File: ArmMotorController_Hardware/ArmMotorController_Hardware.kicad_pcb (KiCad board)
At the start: 2 copper layers, 98 parts, among them SW1 SW_Push, SW2 SW_Push, SW3 SW_Push, SW4 SW_Push, SW5 SW_SPDT, U1 AP1059, U2 AP1059, U3 TM4C129E_Launchpad, U4 MAX_3232, U5 VNH5019A_E, U6 VNH5019A_E, U7 VNH5019A_E, U8 VNH5019A_E

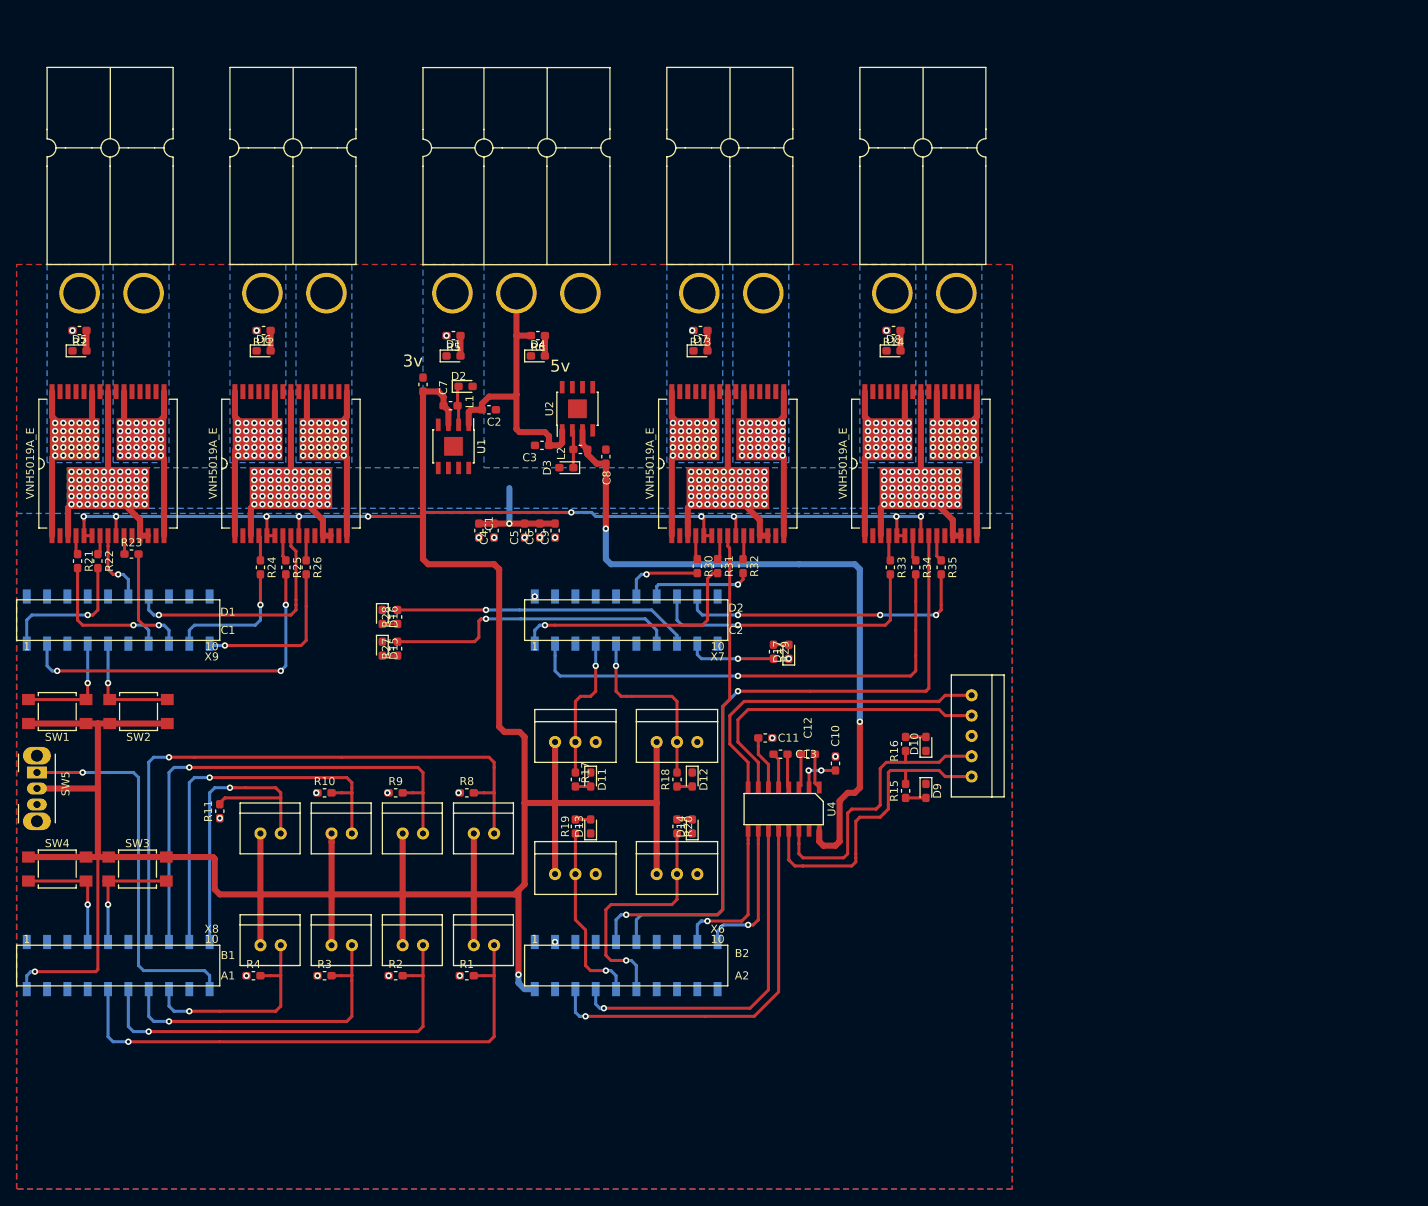
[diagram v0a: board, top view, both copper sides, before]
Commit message: Added text above the VNH's
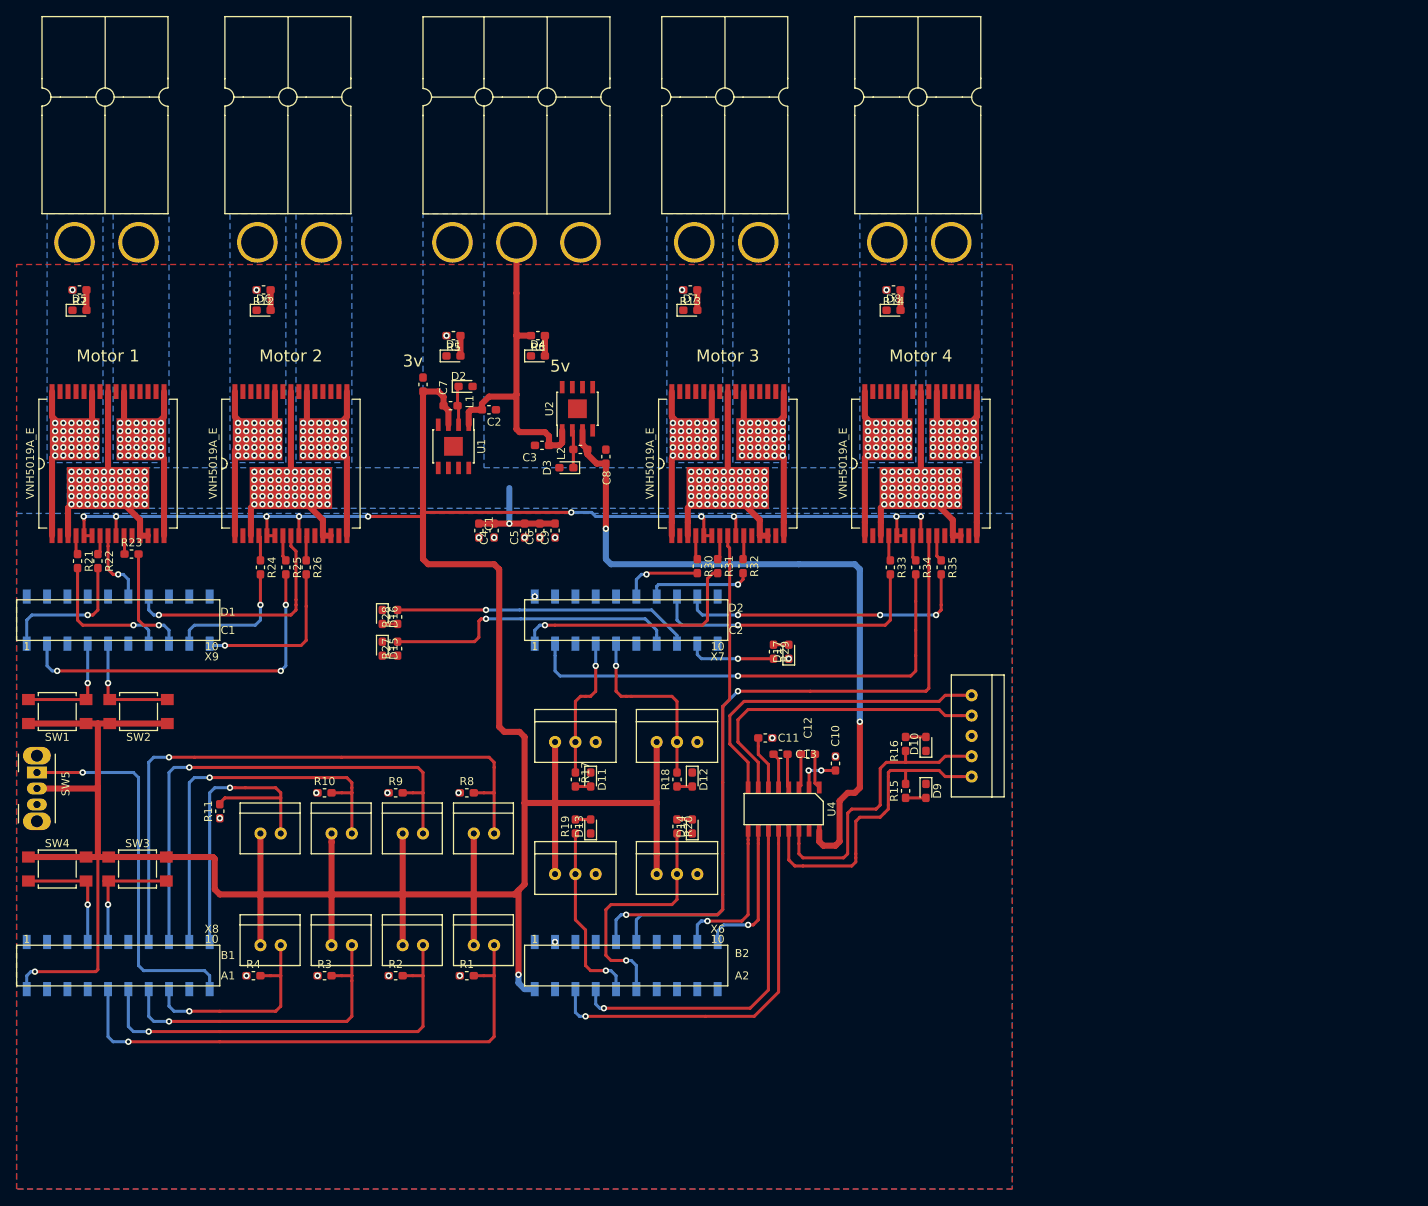
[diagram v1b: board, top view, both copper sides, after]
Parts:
- moved Conn17 6.38 mm to (65.4, 41.9)
- moved Conn18 6.38 mm to (120.0, 41.9)
- moved Conn16 6.38 mm to (42.5, 41.9)
- moved Conn19 6.38 mm to (144.1, 41.9)
- moved Conn1 6.35 mm to (90.2, 41.9)
- moved D7 5.24 mm to (123.6, 54.0)
- moved R13 5.24 mm to (123.6, 51.4)
- moved D5 5.08 mm to (47.2, 54.0)
- moved D6 5.08 mm to (70.2, 54.0)
- moved D8 5.08 mm to (149.0, 54.0)
- moved R12 5.08 mm to (70.2, 51.4)
- moved R14 5.08 mm to (149.0, 51.4)
- moved R7 5.08 mm to (47.2, 51.4)
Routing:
- net 12vLog: track 36.6 -> 43.0 mm
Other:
- board text added: "Motor 1"
- board text added: "Motor 2"
- board text added: "Motor 3"
- board text added: "Motor 4"

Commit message: save
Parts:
- moved D1 5.08 mm to (94.0, 54.6)
- moved R5 5.08 mm to (94.0, 52.1)
- moved D8 0.64 mm to (148.3, 54.0)
- moved R14 0.64 mm to (148.3, 51.4)
- moved D6 0.64 mm to (69.6, 54.0)
- moved D7 0.64 mm to (124.2, 54.0)
- moved R12 0.64 mm to (69.6, 51.4)
- moved R13 0.64 mm to (124.2, 51.4)
- moved D5 0.63 mm to (46.6, 54.0)
- moved R7 0.63 mm to (46.6, 51.4)
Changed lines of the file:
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@@
   )
   (setup
-    (last_trace_width 0.762)
+    (last_trace_width 0.25)
     (user_trace_width 0.254)
     (user_trace_width 0.381)
@@
   )
   (module Resistor_SMD:R_0603_1608Metric_Pad1.05x0.95mm_HandSolder (layer F.Cu)
-    (at 148.985 51.435 180)
+    (at 148.35 51.435 180)
     (descr "Resistor SMD 0603 (1608 Metric), square (rectangular) end terminal, IPC_7351 nominal with elongated pad for handsoldering. (Body size source: http://www.tortai-tech.com/upload/download/2011102023233369053.pdf), generated with kicad-footprint-generator")
     (tags "resistor handsolder")
@@
   )
   (module Resistor_SMD:R_0603_1608Metric_Pad1.05x0.95mm_HandSolder (layer F.Cu)
-    (at 123.585 51.435 180)
+    (at 124.22 51.435 180)
     (descr "Resistor SMD 0603 (1608 Metric), square (rectangular) end terminal, IPC_7351 nominal with elongated pad for handsoldering. (Body size source: http://www.tortai-tech.com/upload/download/2011102023233369053.pdf), generated with kicad-footprint-generator")
     (tags "resistor handsolder")
@@
   )
   (module Resistor_SMD:R_0603_1608Metric_Pad1.05x0.95mm_HandSolder (layer F.Cu)
-    (at 70.245 51.435 180)
+    (at 69.61 51.435 180)
     (descr "Resistor SMD 0603 (1608 Metric), square (rectangular) end terminal, IPC_7351 nominal with elongated pad for handsoldering. (Body size source: http://www.tortai-tech.com/upload/download/2011102023233369053.pdf), generated with kicad-footprint-generator")
     (tags "resistor handsolder")
@@
   )
   (module LED_SMD:LED_0603_1608Metric_Pad1.05x0.95mm_HandSolder (layer F.Cu)
-    (at 70.245 53.975)
+    (at 69.61 53.975)
     (descr "LED SMD 0603 (1608 Metric), square (rectangular) end terminal, IPC_7351 nominal, (Body size source: http://www.tortai-tech.com/upload/download/2011102023233369053.pdf), generated with kicad-footprint-generator")
     (tags "LED handsolder")
@@
   )
   (module LED_SMD:LED_0603_1608Metric_Pad1.05x0.95mm_HandSolder (layer F.Cu)
-    (at 148.985 53.975)
+    (at 148.35 53.975)
     (descr "LED SMD 0603 (1608 Metric), square (rectangular) end terminal, IPC_7351 nominal, (Body size source: http://www.tortai-tech.com/upload/download/2011102023233369053.pdf), generated with kicad-footprint-generator")
     (tags "LED handsolder")
@@
   )
   (module LED_SMD:LED_0603_1608Metric_Pad1.05x0.95mm_HandSolder (layer F.Cu)
-    (at 47.23 53.975)
+    (at 46.595 53.975)
     (descr "LED SMD 0603 (1608 Metric), square (rectangular) end terminal, IPC_7351 nominal, (Body size source: http://www.tortai-tech.com/upload/download/2011102023233369053.pdf), generated with kicad-footprint-generator")
     (tags "LED handsolder")
@@
   )
   (module LED_SMD:LED_0603_1608Metric_Pad1.05x0.95mm_HandSolder (layer F.Cu)
-    (at 123.585 53.975)
+    (at 124.22 53.975)
     (descr "LED SMD 0603 (1608 Metric), square (rectangular) end terminal, IPC_7351 nominal, (Body size source: http://www.tortai-tech.com/upload/download/2011102023233369053.pdf), generated with kicad-footprint-generator")
     (tags "LED handsolder")
@@
   )
   (module Resistor_SMD:R_0603_1608Metric_Pad1.05x0.95mm_HandSolder (layer F.Cu)
-    (at 93.98 57.15 180)
+    (at 93.98 52.07 180)
     (descr "Resistor SMD 0603 (1608 Metric), square (rectangular) end terminal, IPC_7351 nominal with elongated pad for handsoldering. (Body size source: http://www.tortai-tech.com/upload/download/2011102023233369053.pdf), generated with kicad-footprint-generator")
     (tags "resistor handsolder")
@@
   )
   (module Resistor_SMD:R_0603_1608Metric_Pad1.05x0.95mm_HandSolder (layer F.Cu)
-    (at 47.23 51.435 180)
+    (at 46.595 51.435 180)
     (descr "Resistor SMD 0603 (1608 Metric), square (rectangular) end terminal, IPC_7351 nominal with elongated pad for handsoldering. (Body size source: http://www.tortai-tech.com/upload/download/2011102023233369053.pdf), generated with kicad-footprint-generator")
     (tags "resistor handsolder")
@@
   )
   (module LED_SMD:LED_0603_1608Metric_Pad1.05x0.95mm_HandSolder (layer F.Cu)
-    (at 93.98 59.69)
+    (at 93.98 54.61)
     (descr "LED SMD 0603 (1608 Metric), square (rectangular) end terminal, IPC_7351 nominal, (Body size source: http://www.tortai-tech.com/upload/download/2011102023233369053.pdf), generated with kicad-footprint-generator")
     (tags "LED handsolder")
@@
   (segment (start 65.405 114.935) (end 64.77 115.57) (width 0.381) (layer F.Cu) (net 16))
   (segment (start 72.39 114.935) (end 65.405 114.935) (width 0.381) (layer F.Cu) (net 16))
-  (segment (start 94.855 57.15) (end 94.855 59.69) (width 0.762) (layer F.Cu) (net 17))
+  (segment (start 94.855 52.07) (end 94.855 54.61) (width 0.762) (layer F.Cu) (net 17))
   (segment (start 134.62 119.032) (end 134.62 120.65) (width 0.381) (layer F.Cu) (net 31))
   (segment (start 134.62 120.65) (end 134.62 139.192) (width 0.381) (layer F.Cu) (net 31))
@@
   (segment (start 108.966 73.406) (end 108.966 71.374) (width 0.381) (layer F.Cu) (net 74))
   (segment (start 105.41 57.15) (end 105.41 59.69) (width 0.762) (layer F.Cu) (net 75))
-  (segment (start 48.105 51.435) (end 48.105 53.975) (width 0.762) (layer F.Cu) (net 76))
-  (segment (start 71.12 51.435) (end 71.12 53.975) (width 0.762) (layer F.Cu) (net 77))
-  (segment (start 124.46 51.435) (end 124.46 53.975) (width 0.762) (layer F.Cu) (net 78))
-  (segment (start 149.86 51.435) (end 149.86 53.975) (width 0.762) (layer F.Cu) (net 79))
+  (segment (start 47.47 51.435) (end 47.47 53.975) (width 0.762) (layer F.Cu) (net 76))
+  (segment (start 70.485 51.435) (end 70.485 53.975) (width 0.762) (layer F.Cu) (net 77))
+  (segment (start 125.095 51.435) (end 125.095 53.975) (width 0.762) (layer F.Cu) (net 78))
+  (segment (start 149.225 51.435) (end 149.225 53.975) (width 0.762) (layer F.Cu) (net 79))
   (segment (start 150.495 114.935) (end 153.035 114.935) (width 0.381) (layer F.Cu) (net 80))
   (segment (start 150.495 107.315) (end 153.035 107.315) (width 0.381) (layer F.Cu) (net 81))
@@
   (segment (start 85.09 93.19) (end 86.995 93.19) (width 0.381) (layer F.Cu) (net 87))
   (segment (start 133.985 95.786) (end 135.89 95.786) (width 0.381) (layer F.Cu) (net 88))
-  (via (at 93.105 57.15) (size 0.8) (drill 0.4) (layers F.Cu B.Cu) (net 89))
+  (via (at 93.105 52.07) (size 0.8) (drill 0.4) (layers F.Cu B.Cu) (net 89))
   (via (at 149.86 76.2) (size 0.8) (drill 0.4) (layers F.Cu B.Cu) (net 89))
   (via (at 150.876 78.232) (size 0.8) (drill 0.4) (layers F.Cu B.Cu) (net 89))
@@
   (segment (start 100.965 80.645) (end 100.965 76.2) (width 0.762) (layer B.Cu) (net 89))
   (segment (start 156.4 82.1563) (end 157.4 82.1563) (width 0.762) (layer F.Cu) (net 89))
-  (via (at 46.355 51.435) (size 0.8) (drill 0.4) (layers F.Cu B.Cu) (net 90))
+  (via (at 45.72 51.435) (size 0.8) (drill 0.4) (layers F.Cu B.Cu) (net 90))
   (via (at 44.196 72.136) (size 0.8) (drill 0.4) (layers F.Cu B.Cu) (net 90))
   (via (at 45.212 72.136) (size 0.8) (drill 0.4) (layers F.Cu B.Cu) (net 90))
@@
   (segment (start 46.1518 70.104) (end 43.800001 72.455799) (width 0.762) (layer F.Cu) (net 90))
   (segment (start 46.6344 70.104) (end 46.1518 70.104) (width 0.762) (layer F.Cu) (net 90))
-  (via (at 69.37 51.435) (size 0.8) (drill 0.4) (layers F.Cu B.Cu) (net 91))
-  (via (at 122.555 51.435) (size 0.8) (drill 0.4) (layers F.Cu B.Cu) (net 92))
-  (via (at 148.11 51.435) (size 0.8) (drill 0.4) (layers F.Cu B.Cu) (net 93))
+  (via (at 68.735 51.435) (size 0.8) (drill 0.4) (layers F.Cu B.Cu) (net 91))
+  (via (at 123.19 51.435) (size 0.8) (drill 0.4) (layers F.Cu B.Cu) (net 92))
+  (via (at 147.475 51.435) (size 0.8) (drill 0.4) (layers F.Cu B.Cu) (net 93))
   (segment (start 109.22 104.14) (end 109.22 107.95) (width 0.381) (layer F.Cu) (net 94))
   (segment (start 109.22 104.14) (end 109.22 102.87) (width 0.381) (layer F.Cu) (net 94))
@@
     (polygon
       (pts
-        (xy 163.83 48.26) (xy 163.83 163.83) (xy 39.37 163.83) (xy 39.37 48.26)
+        (xy 163.83 41.91) (xy 163.83 163.83) (xy 39.37 163.83) (xy 39.37 41.91)
       )
     )
